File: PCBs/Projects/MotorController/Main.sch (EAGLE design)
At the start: 116 parts, among them Q1 ZXMP10A17GQ, Q2 MMBT5551LT1G, Q3 BUK9240-100A.118, Q4 BUK9240-100A.118, U1 DRV8301, U11 LT4356-2, U2 ESDA6V1SC6Y, U3 ESDA6V1SC6Y, U4 TMP101, U5 ACS758LCB, U6 ESDA6V1SC6Y, U7 MTI85W100GC, U8 ESDA6V1SC6Y

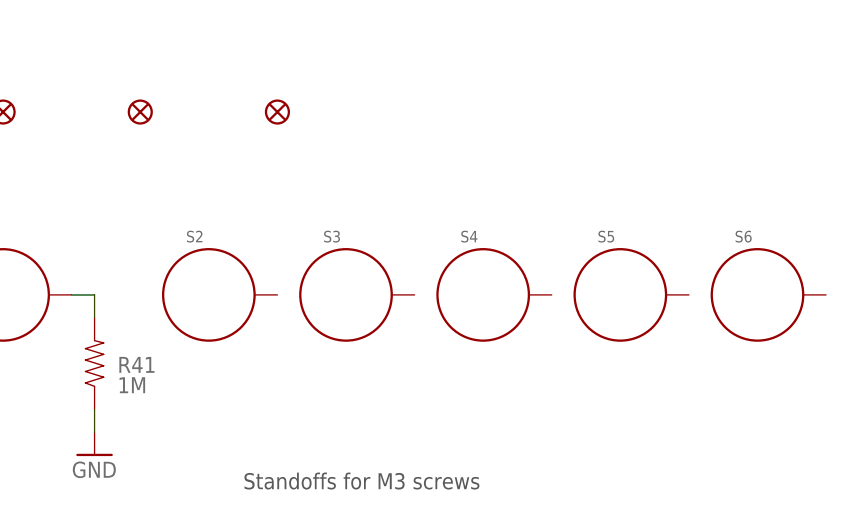
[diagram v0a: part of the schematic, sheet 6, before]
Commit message: fixed a couple airwires -Added keepout below 1206 resistors -TODO: current path from power input to fets needs to bet larger -TODO: silk screen fixes -TODO: DRV8301 solder mask fix -TODO: Mounting hole placement -TODO: interior layer placement
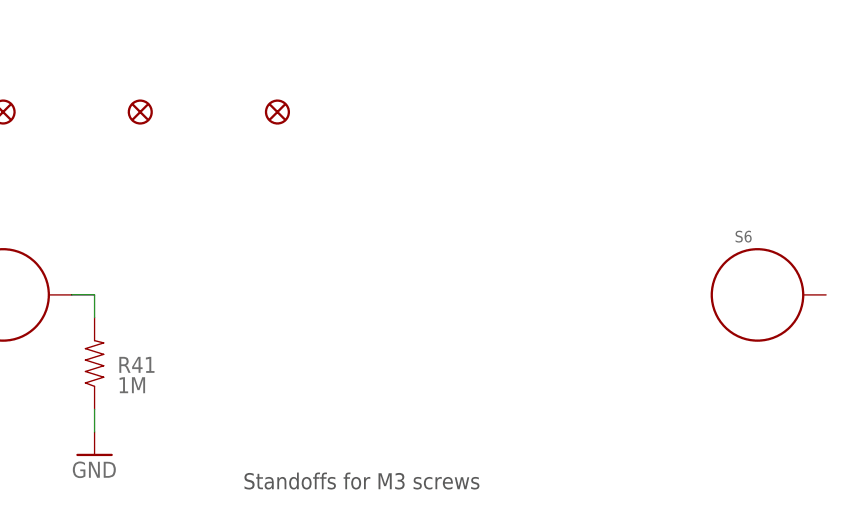
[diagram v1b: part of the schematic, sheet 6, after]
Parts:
- removed S2, S3, S4, S5: STANDOFF_ELECTRICAL, SparkFun-Electromechanical:STANDOFF_ELECTRICAL
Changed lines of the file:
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@@
 <part name="L1" library="SparkFun-Passives" deviceset="INDUCTOR" device="SRP7050TA-220M" value="22u"/>
 <part name="S1" library="SparkFun-Electromechanical" deviceset="STANDOFF_ELECTRICAL" device=""/>
-<part name="S2" library="SparkFun-Electromechanical" deviceset="STANDOFF_ELECTRICAL" device=""/>
-<part name="S3" library="SparkFun-Electromechanical" deviceset="STANDOFF_ELECTRICAL" device=""/>
-<part name="S4" library="SparkFun-Electromechanical" deviceset="STANDOFF_ELECTRICAL" device=""/>
-<part name="S5" library="SparkFun-Electromechanical" deviceset="STANDOFF_ELECTRICAL" device=""/>
 <part name="S6" library="SparkFun-Electromechanical" deviceset="STANDOFF_ELECTRICAL" device=""/>
 <part name="R41" library="SparkFun-Resistors" deviceset="RESISTOR" device="1206" value="1M"/>
@@
 <instance part="FD6" gate="G$1" x="71.12" y="243.84"/>
 <instance part="S1" gate="G$1" x="40.64" y="223.52"/>
-<instance part="S2" gate="G$1" x="63.5" y="223.52"/>
-<instance part="S3" gate="G$1" x="78.74" y="223.52"/>
-<instance part="S4" gate="G$1" x="93.98" y="223.52"/>
-<instance part="S5" gate="G$1" x="109.22" y="223.52"/>
 <instance part="S6" gate="G$1" x="124.46" y="223.52"/>
 <instance part="R41" gate="G$1" x="50.8" y="215.9" smashed="yes" rot="R90">

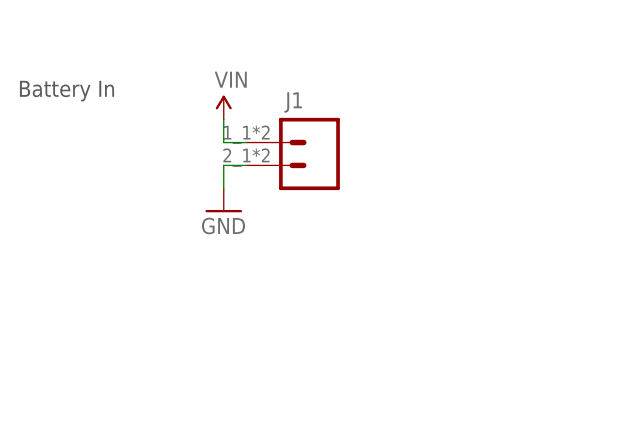
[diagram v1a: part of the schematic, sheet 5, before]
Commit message: Fixed current path concerns -Arranged top fiducials
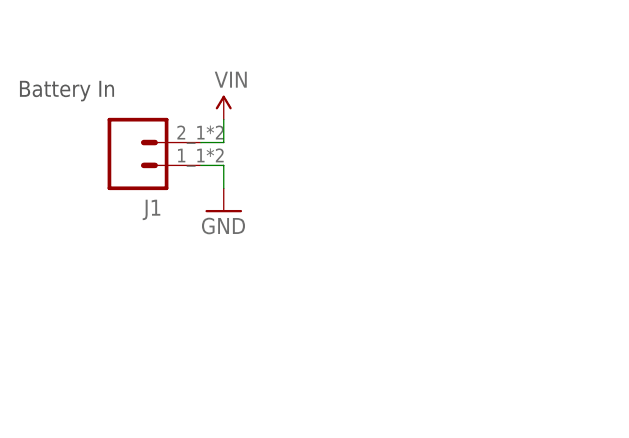
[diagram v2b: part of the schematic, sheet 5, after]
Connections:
- net GND: now also J1.1; no longer J1.2
- net VIN: now also J1.2; no longer J1.1
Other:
- moved on the sheet: J1
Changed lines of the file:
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@@
 <instance part="SUPPLY24" gate="G$1" x="76.2" y="218.44"/>
 <instance part="GND25" gate="1" x="76.2" y="208.28"/>
-<instance part="J1" gate="G$1" x="86.36" y="215.9" smashed="yes" rot="R180">
-<attribute name="VALUE" x="88.9" y="220.98" size="1.778" layer="96" rot="R180"/>
-<attribute name="NAME" x="85.09" y="221.488" size="1.778" layer="95" rot="R180"/>
+<instance part="J1" gate="G$1" x="66.04" y="213.36" smashed="yes">
+<attribute name="VALUE" x="63.5" y="208.28" size="1.778" layer="96"/>
+<attribute name="NAME" x="67.31" y="207.772" size="1.778" layer="95"/>
 </instance>
 <instance part="J5" gate="G$1" x="248.92" y="213.36"/>
@@
 <pinref part="GND25" gate="1" pin="GND"/>
 <wire x1="76.2" y1="210.82" x2="76.2" y2="213.36" width="0.4064" layer="91"/>
-<pinref part="J1" gate="G$1" pin="2"/>
-<wire x1="78.74" y1="213.36" x2="76.2" y2="213.36" width="0.4064" layer="91"/>
+<pinref part="J1" gate="G$1" pin="1"/>
+<wire x1="76.2" y1="213.36" x2="73.66" y2="213.36" width="0.4064" layer="91"/>
 </segment>
 <segment>
@@
 <pinref part="SUPPLY24" gate="G$1" pin="VIN"/>
 <wire x1="76.2" y1="215.9" x2="76.2" y2="218.44" width="0.4064" layer="91"/>
-<pinref part="J1" gate="G$1" pin="1"/>
-<wire x1="78.74" y1="215.9" x2="76.2" y2="215.9" width="0.4064" layer="91"/>
+<pinref part="J1" gate="G$1" pin="2"/>
+<wire x1="73.66" y1="215.9" x2="76.2" y2="215.9" width="0.4064" layer="91"/>
 </segment>
 </net>

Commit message: Lots of fine detail work -Mounting holes placed -Silk fixes and additions -SEM added to board
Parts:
- removed FD4: FIDUCIAL1X2, SparkFun-Aesthetics:FIDUCIAL1X2
- removed R45, R46, R47: 100, SparkFun-Resistors:RESISTOR0805-RES
- removed SJ4: SOLDERJUMPERTRACE, SparkFun-Retired:SOLDERJUMPERTRACE
- added C29: 0.01u, SparkFun-Capacitors:CAP0805
- added FD1: FIDUCIAL1X2, SparkFun-Aesthetics:FIDUCIAL1X2
- added R26: 330, SparkFun-Resistors:RESISTOR0805-RES
- added R27: 100, SparkFun-Resistors:RESISTOR0805-RES
- added R43: 1M, SparkFun-Resistors:RESISTOR1206
- added S2, S3: STANDOFF_ELECTRICAL, SparkFun-Electromechanical:STANDOFF_ELECTRICAL
- added SJ3: SOLDERJUMPERNO, SparkFun-Retired:SOLDERJUMPERNO
- R22, R23: value 330 -> 100
- R25: value 100 -> 330
- R31: value 510k -> 100
- R32: value 1k -> 100
- R33: value 1k -> 510k
- R34, R35: value 4.7k -> 1k
- R36, R37: value 10k -> 4.7k
- R39: value 100k -> 10k; device SparkFun-Resistors:RESISTOR1206 -> SparkFun-Resistors:RESISTOR0805-RES
- R40: value 5.1k -> 10k; device SparkFun-Resistors:RESISTOR1206 -> SparkFun-Resistors:RESISTOR0805-RES
- R41: value 1M -> 100k
- R42: value 100 -> 5.1k; device SparkFun-Resistors:RESISTOR0805-RES -> SparkFun-Resistors:RESISTOR1206
- SJ2: value SOLDERJUMPERNO -> SOLDERJUMPERTRACE; device SparkFun-Retired:SOLDERJUMPERNO -> SparkFun-Retired:SOLDERJUMPERTRACE
- U4: value TMP101 -> ESDA6V1SC6Y; device SparkFun-DigitalIC:TMP101 -> IC:ESDA6V1SC6Y
- U5: value ACS758LCB -> TMP101; device IC:ACS758LCB -> SparkFun-DigitalIC:TMP101
- U6: value ESDA6V1SC6Y -> ACS758LCB; device IC:ESDA6V1SC6Y -> IC:ACS758LCB
- U7: value MTI85W100GC -> ESDA6V1SC6Y; device IC:MTI85W100GC -> IC:ESDA6V1SC6Y
- U8: value ESDA6V1SC6Y -> MTI85W100GC; device IC:ESDA6V1SC6Y -> IC:MTI85W100GC
- renumbered FD6 to FD3, J6 to J4, MOD2 to MOD1, R44 to R28, S6 to S4
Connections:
- net !IN-FAULT: now also MOD1.P1_1
- net 5V: now also R39.1, R40.1, SJ3.2, U5.V+, U6.VCC, U7.IO1; no longer R32.1, R35.1, SJ2.2, U4.V+, U5.VCC, U6.IO1
- net A: now also U8.L1, U8.S1; no longer U7.L1, U7.S1
- net B: now also U8.L2, U8.S3; no longer U7.L2, U7.S3
- net C: now also U8.L3, U8.S5; no longer U7.L3, U7.S5
- net DISABLE: now also R23.1; no longer R42.1
- net DISP_OUT: now also R22.1, U4.IO3; no longer R21.1, U3.IO3
- net GH_A: now also U8.G1; no longer U7.G1
- net GH_B: now also U8.G3; no longer U7.G3
- net GH_C: now also U8.G5; no longer U7.G5
- net GL_A: now also U8.G2; no longer U7.G2
- net GL_B: now also U8.G4; no longer U7.G4
- net GL_C: now also U8.G6; no longer U7.G6
- net GND: now also C29.2, R35.2, R42.1, R43.1, U5.ADD0, U7.GND, U8.L-, U8.S2, U8.S4, U8.S6; no longer R31.2, R40.1, R41.1, U4.ADD0, U7.L-, U7.S2, U7.S4, U7.S6, U8.GND
- net GPIO_TBD: now also U4.IO4; no longer U3.IO4
- net H1: now also R38.2, U7.IO2; no longer R36.2, U6.IO2
- net H2: now also R29.1, R39.2, U7.IO3; no longer R37.2, R45.1, U6.IO3
- net H3: now also R30.1, R40.2, U7.IO4; no longer R38.2, R46.1, U6.IO4
- net ISENSE: now also U3.IO3, U6.VIOUT; no longer U5.VIOUT, U8.IO3
- net MONITOR_RX: now also R32.1, U4.IO2; no longer R30.1, U3.IO2
- net MONITOR_TX: now also R31.1, U4.IO1; no longer R29.1, U3.IO1
- net N$16: now also R23.2; no longer R42.2
- net N$31: now also C29.1, R43.2; no longer R41.2
- net N$32: now also R26.1; no longer R24.1
- net N$33: now also R25.1; no longer R23.1
- net N$34: now also R24.1; no longer R22.1
- net N$35: now also R26.2; no longer R24.2
- net N$36: now also R25.2; no longer R23.2
- net N$37: now also R24.2; no longer R22.2
- net N$39: now also R27.2; no longer R25.2
- net N$41: now also R22.2; no longer R21.2
- net N$43: now also R31.2; no longer R29.2
- net N$44: now also R32.2; no longer R30.2
- net N$45: now also SJ2.2; no longer SJ4.2
- net N$47: now also R29.2; no longer R45.2
- net N$48: now also R30.2; no longer R46.2
- net N$49: now also R21.2; no longer R47.2
- net PREJUMP_5V: now also SJ3.1; no longer SJ2.1
- net PWRGD: now also SJ2.1; no longer SJ4.1
- net REVERSE: now also R21.1; no longer R47.1
- net SCL: now also R36.2, U5.SCL; no longer R34.2, U4.SCL
- net SDA: now also R37.2, U5.SDA; no longer R35.2, U4.SDA
- net THROTTLE_1: now also R34.2; no longer R32.2
- net THROTTLE_2: now also R27.1, R33.1; no longer R25.1, R31.1
- net THROTTLE_3: now also R35.1; no longer R33.1
- net T_ALERT: now also U5.ALERT; no longer U4.ALERT
- net VCC: now also R41.2; no longer R39.2
- net VIN: now also U6.IP+; no longer U5.IP+
- net VSENSE: now also R41.1, R42.2, U3.IO1; no longer R39.1, R40.2, U8.IO1
- net V_BATT: now also U6.IP-, U8.L+; no longer U5.IP-, U7.L+

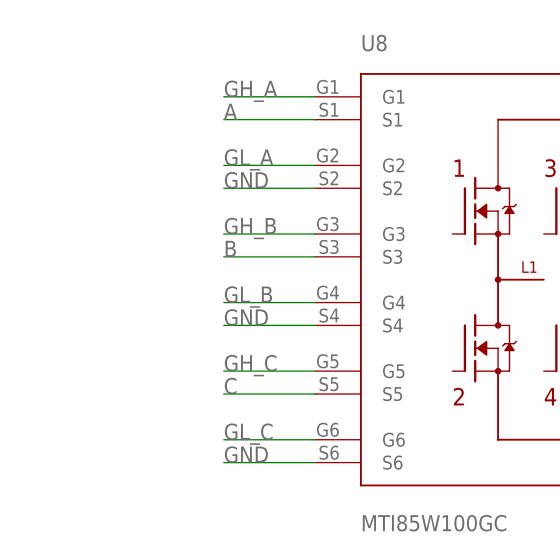
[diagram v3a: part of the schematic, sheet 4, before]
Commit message: Laundry list of fixes -Changed feedback point for buck convert -Labeled layers in copper -Added filter cap to current sense line -Fixed footprint of acs758
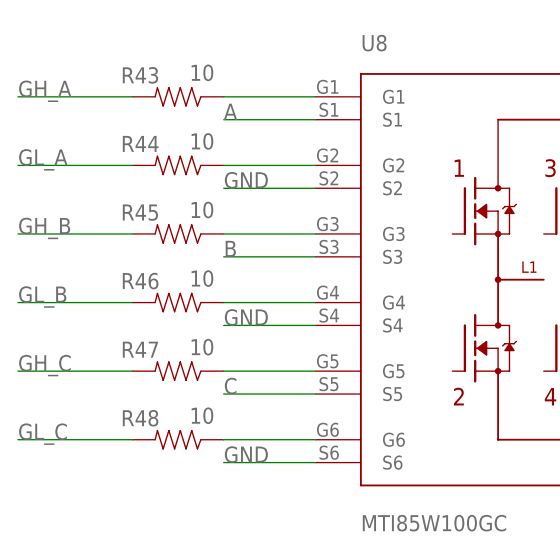
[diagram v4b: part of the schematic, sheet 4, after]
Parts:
- added C30: 0.01u, SparkFun-Capacitors:CAP0805
- added R44, R45, R46, R47, R48: 10, SparkFun-Resistors:RESISTOR0805-RES
- added R49: 1M, SparkFun-Resistors:RESISTOR1206
- C28: value 0.1u -> 10n
- C29: value 0.01u -> 0.1u
- R43: value 1M -> 10; device SparkFun-Resistors:RESISTOR1206 -> SparkFun-Resistors:RESISTOR0805-RES
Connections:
- new net N$27: R45.1, U8.G3
- new net N$28: R43.1, U8.G1
- new net N$38: R44.1, U8.G2
- new net N$50: R46.1, U8.G4
- new net N$51: R47.1, U8.G5
- new net N$52: R48.1, U8.G6
- net 5V: now also C29.1; no longer C28.1, R17.2
- net GH_A: now also R43.2; no longer U8.G1
- net GH_B: now also R45.2; no longer U8.G3
- net GH_C: now also R47.2; no longer U8.G5
- net GL_A: now also R44.2; no longer U8.G2
- net GL_B: now also R46.2; no longer U8.G4
- net GL_C: now also R48.2; no longer U8.G6
- net GND: now also C30.2, R49.1; no longer R43.1
- net IND_LOOP_OUT: now also R17.2
- net ISENSE: now also C28.1
- net N$31: now also C30.1, R49.2; no longer C29.1, R43.2
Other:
- moved on the sheet: C28

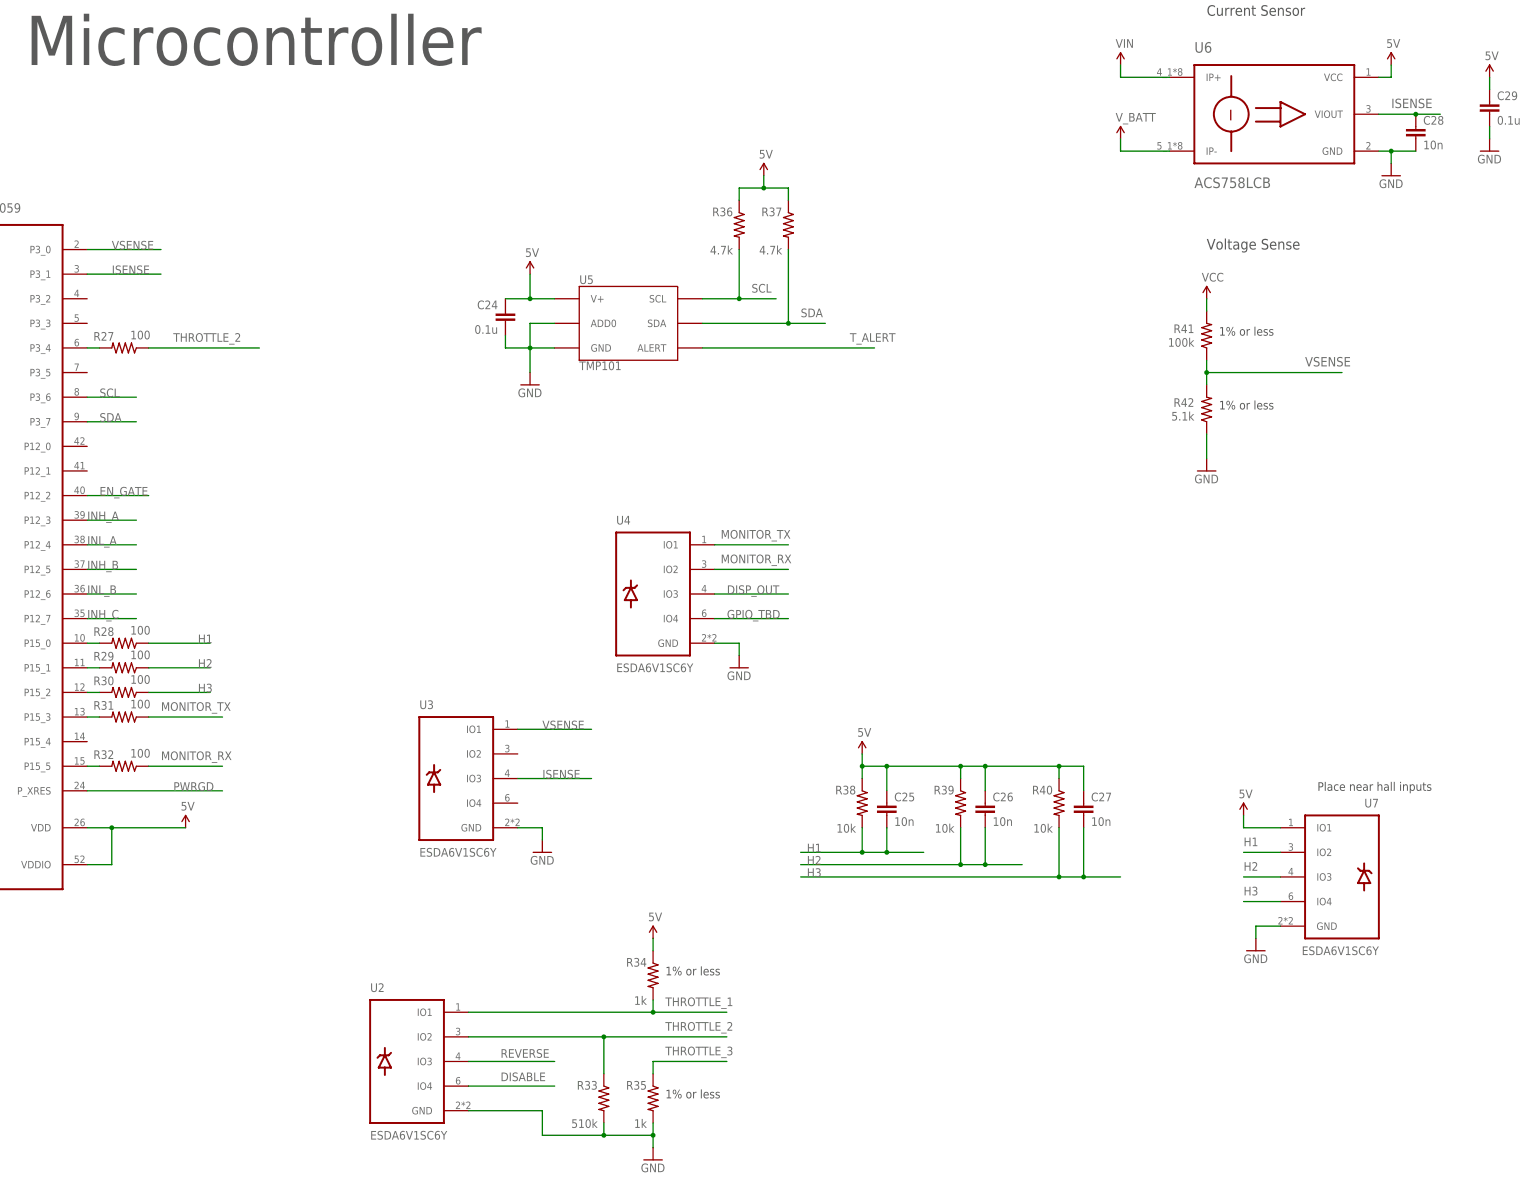
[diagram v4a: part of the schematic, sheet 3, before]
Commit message: Footprint updates and drc fixes -Additionally, filter cap added to throttle
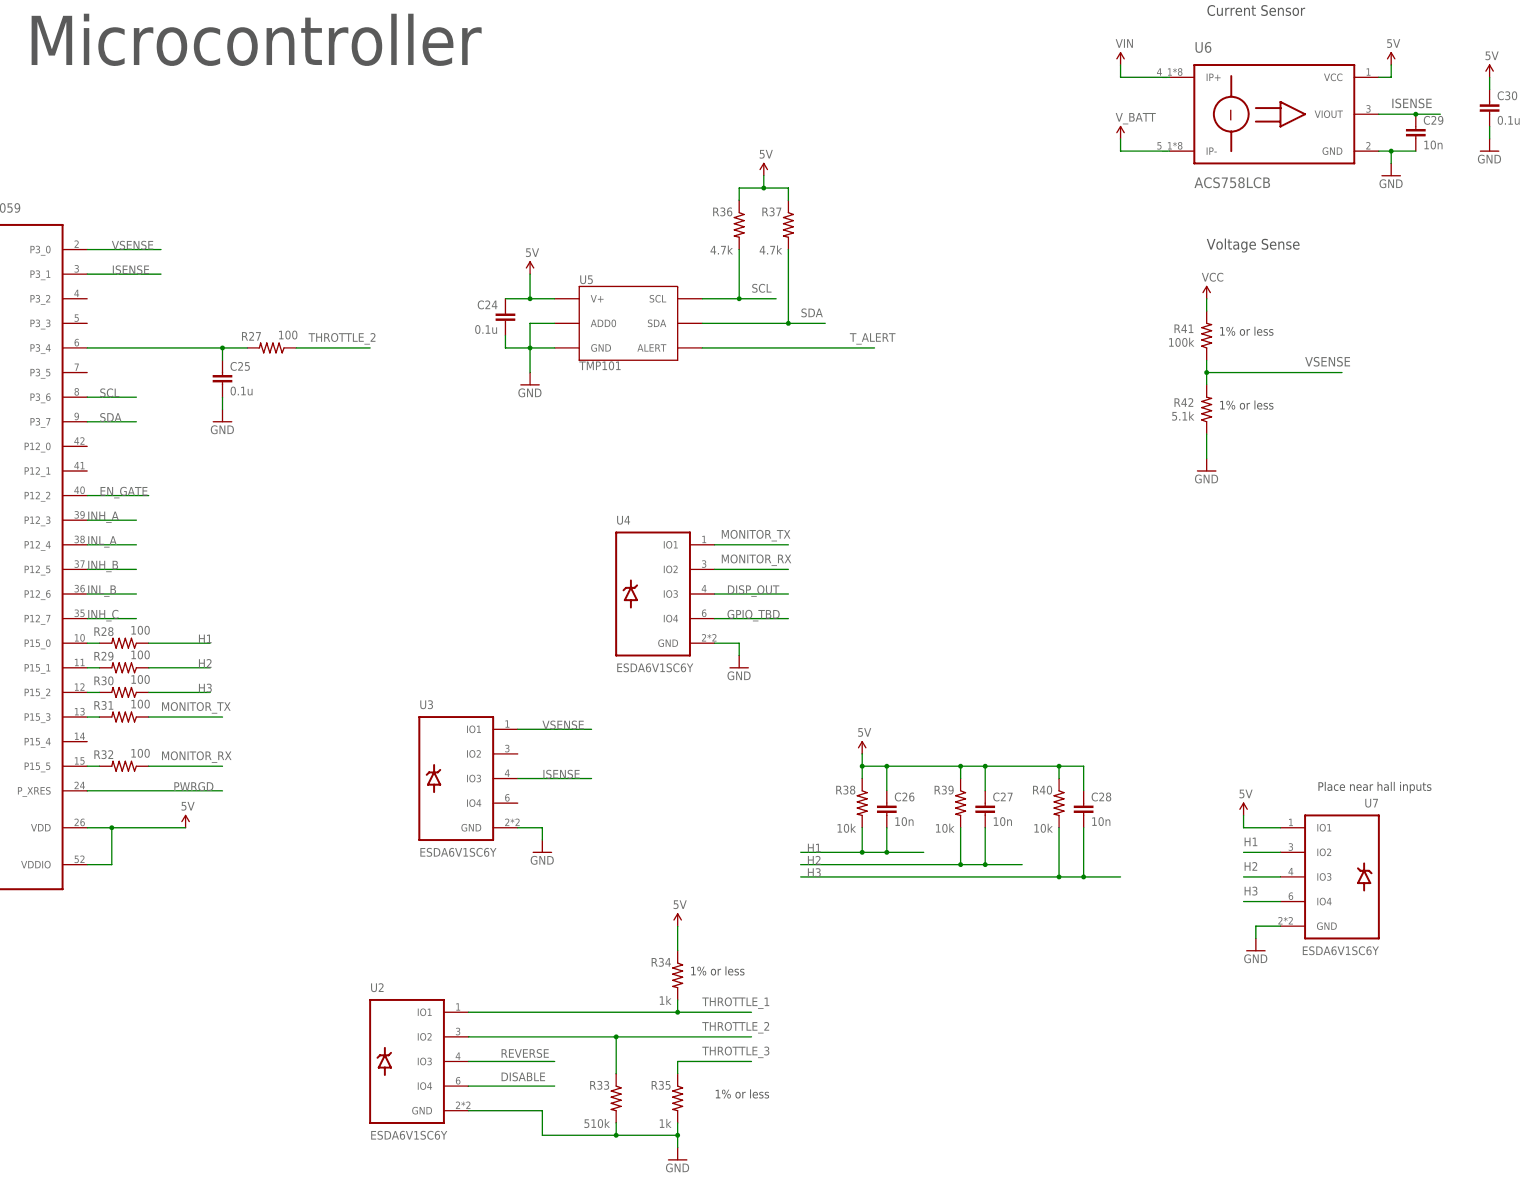
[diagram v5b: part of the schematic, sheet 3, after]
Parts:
- added C31: 0.01u, SparkFun-Capacitors:CAP0805
- C25: value 10n -> 0.1u
- C29: value 0.1u -> 10n
- C30: value 0.01u -> 0.1u
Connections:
- net 5V: now also C28.1, C30.1; no longer C25.1, C29.1
- net GND: now also C25.2, C31.2; no longer C28.2
- net H1: now also C26.2; no longer C25.2
- net H2: now also C27.2; no longer C26.2
- net H3: now also C28.2; no longer C27.2
- net ISENSE: now also C29.1; no longer C28.1
- net N$31: now also C31.1; no longer C30.1
- net N$39: now also C25.1
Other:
- moved on the sheet: C25, C26, C27, C28, C29, R27, R33, R34, R35

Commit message: RevA board sent to board house -lots of little silkscreen additions -tmp101 datasheet added -CAM files saved
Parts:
- added FRAME1, FRAME2, FRAME3, FRAME4, FRAME5, FRAME6: FRAME-LEDGER, SparkFun-Aesthetics:FRAME-LEDGER
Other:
- note added: "Connectors"
- note added: "Mechanical"
- note added: "Power Stage"
- note removed: "Bottom Layer"
- moved on the sheet: C24, C25, C26, C27, C28, C29, C30, C31, D1, D6, MOD1, Q1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

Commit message: Added pdfs of RevB schematic and pcb -Cleaned schematic of RevB
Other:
- note added: "Battery Voltage Divider"
- note added: "Chassis ground bleed capacitor and resistor"
- note added: "Freewheeling Diodes"
- note added: "Gate Driver and Buck Conv."
- note added: "Hall-Effect Current Sensor"
- note added: "IO Protection"
- note added: "MCU"
- note added: "Motor Hall Sensor Filters"
- note added: "Notes: -All resistor tolerances 1% unless specified -All capacitors ceramic unless specified"
- note added: "Power FET Module"
- note added: "Temperature Sensor"
- note added: "Throttle Input Divider and Protection"
- note removed: "Current Sensor"
- note removed: "Microcontroller"
- note removed: "Voltage Sense"
- moved on the sheet: C24, C25, C26, C27, C28, C29, C30, D6, J1, J2, J3, J4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
